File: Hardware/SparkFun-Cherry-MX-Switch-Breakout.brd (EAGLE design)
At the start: 19.1 x 19.1 mm, 17 parts

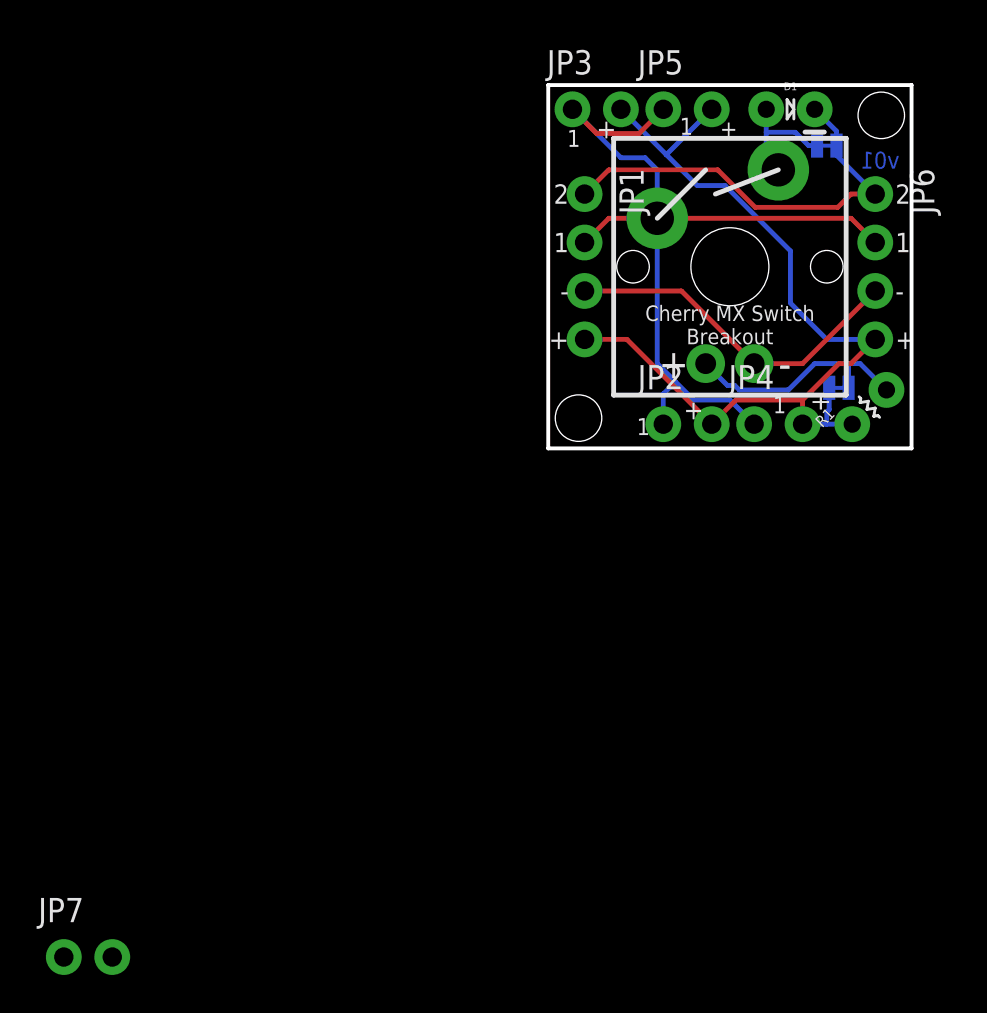
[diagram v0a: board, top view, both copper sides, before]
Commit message: Removing extra 2-pin connector.
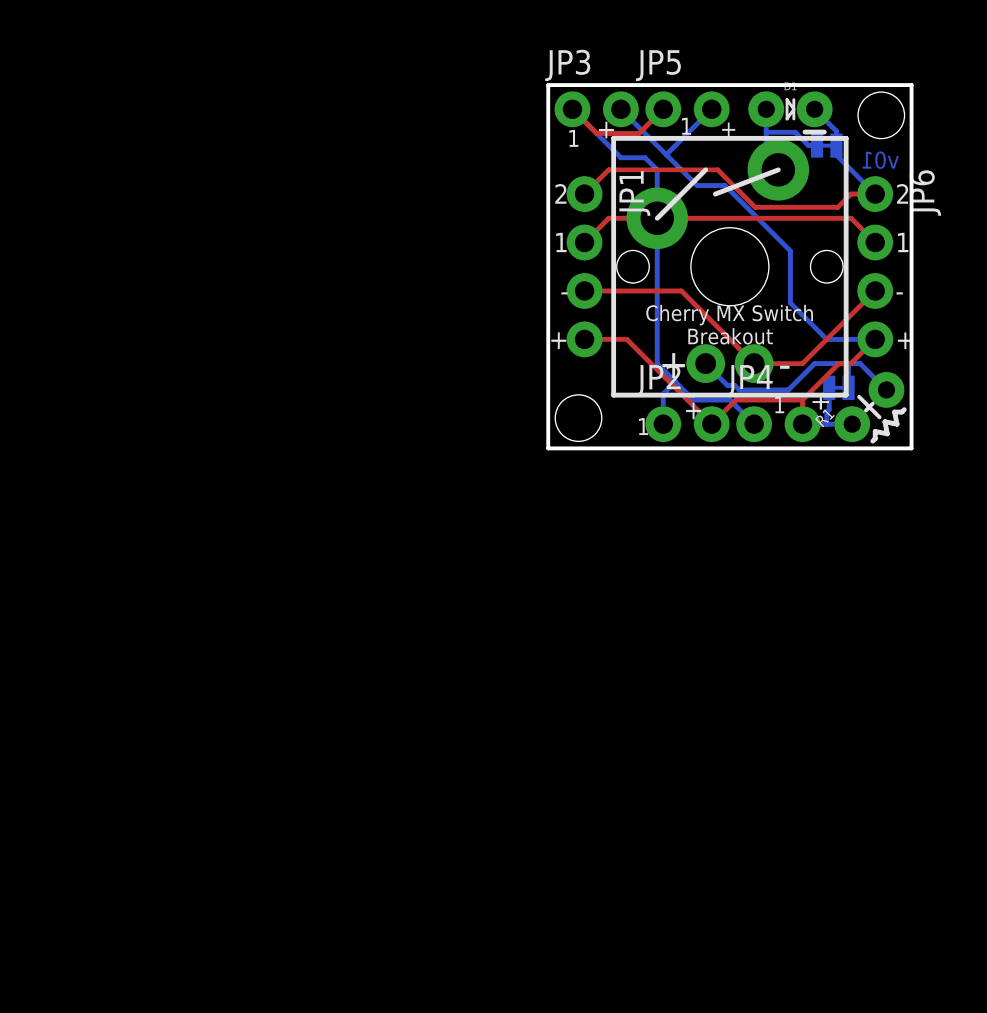
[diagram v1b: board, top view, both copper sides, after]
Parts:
- removed JP7: (no value), SparkFun-Connectors:1X02_NO_SILK
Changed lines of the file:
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@@
 <layer number="47" name="Measures" color="7" fill="1" visible="no" active="yes"/>
 <layer number="48" name="Document" color="7" fill="1" visible="no" active="yes"/>
-<layer number="49" name="Reference" color="7" fill="1" visible="yes" active="yes"/>
+<layer number="49" name="Reference" color="7" fill="1" visible="no" active="yes"/>
 <layer number="50" name="dxf" color="7" fill="1" visible="no" active="no"/>
 <layer number="51" name="tDocu" color="6" fill="1" visible="yes" active="yes"/>
@@
 <wire x1="14.605" y1="3.175" x2="15.875" y2="3.175" width="0.254" layer="30"/>
 <wire x1="15.24" y1="17.399" x2="15.24" y2="18.161" width="0.254" layer="22"/>
+<wire x1="17.018" y1="0.381" x2="17.145" y2="0.508" width="0.254" layer="21"/>
+<wire x1="17.145" y1="0.508" x2="17.145" y2="0.889" width="0.254" layer="21"/>
+<wire x1="17.78" y1="0.762" x2="17.145" y2="0.889" width="0.254" layer="21"/>
+<wire x1="18.669" y1="2.032" x2="18.542" y2="1.905" width="0.254" layer="21"/>
+<wire x1="17.78" y1="0.762" x2="17.653" y2="1.397" width="0.254" layer="21"/>
+<wire x1="18.288" y1="1.27" x2="17.653" y2="1.397" width="0.254" layer="21"/>
+<wire x1="18.288" y1="1.27" x2="18.161" y2="1.905" width="0.254" layer="21"/>
+<wire x1="18.542" y1="1.905" x2="18.161" y2="1.905" width="0.254" layer="21"/>
 </plain>
 <attributes>
@@
 <element name="STANDOFF2" library="cherry-temp" package="STAND-OFF-2-56" value="STAND-OFF2-56" x="1.5875" y="1.5875"/>
 <element name="STANDOFF1" library="cherry-temp" package="STAND-OFF-2-56" value="STAND-OFF2-56" x="17.4625" y="17.4625"/>
-<element name="JP7" library="SparkFun-Connectors" package="1X02_NO_SILK" value="" x="-25.4" y="-26.67"/>
 </elements>
 <signals>

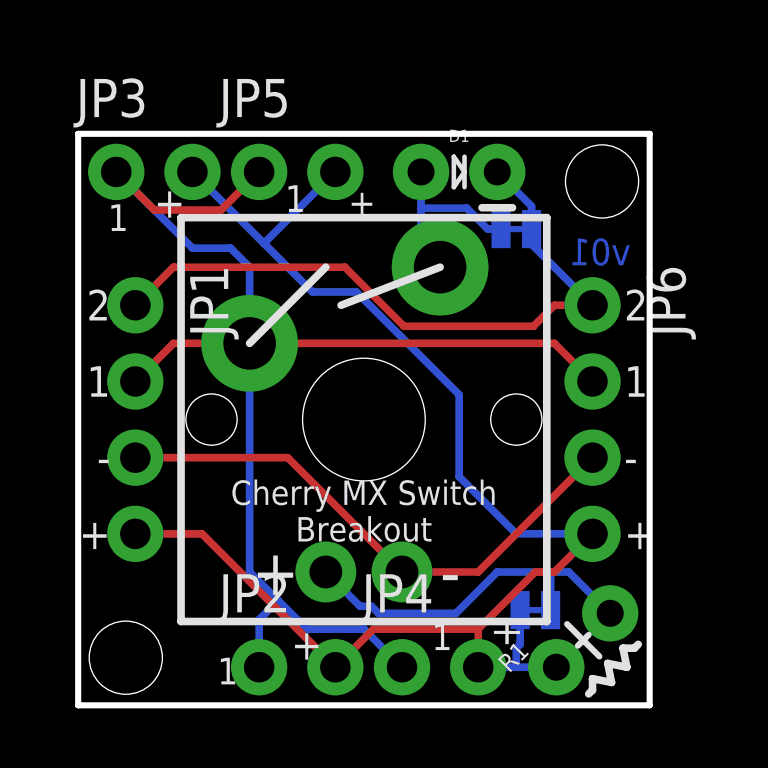
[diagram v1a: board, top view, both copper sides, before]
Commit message: Adjsting some silk, setting version to v10.
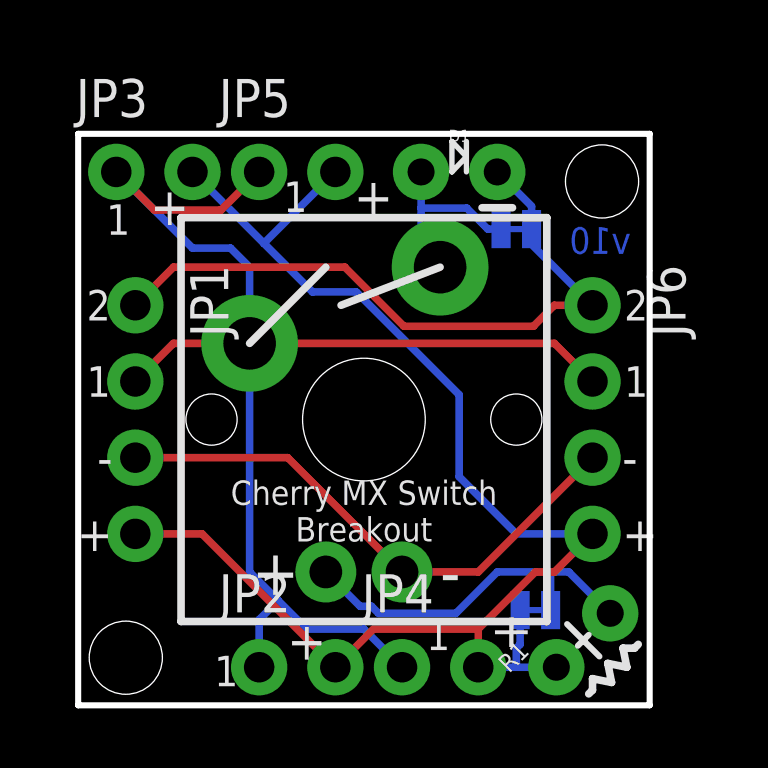
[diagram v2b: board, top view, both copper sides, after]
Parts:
- moved LOGO1 0.57 mm to (4.00, 3.24)
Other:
- board text added: "v10"
- board text removed: "Cherry MX Breakout"
- board text removed: "v01"
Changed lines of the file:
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@@
 <?xml version="1.0" encoding="utf-8"?>
 <!DOCTYPE eagle SYSTEM "eagle.dtd">
-<eagle version="7.1.0">
+<eagle version="7.5.0">
 <drawing>
 <settings>
@@
 <setting verticaltext="up"/>
 </settings>
-<grid distance="0.05" unitdist="inch" unit="inch" style="lines" multiple="1" display="yes" altdistance="0.005" altunitdist="inch" altunit="inch"/>
+<grid distance="0.05" unitdist="inch" unit="inch" style="lines" multiple="1" display="yes" altdistance="0.0025" altunitdist="inch" altunit="inch"/>
 <layers>
 <layer number="1" name="Top" color="4" fill="1" visible="yes" active="yes"/>
@@
 <layer number="47" name="Measures" color="7" fill="1" visible="no" active="yes"/>
 <layer number="48" name="Document" color="7" fill="1" visible="no" active="yes"/>
-<layer number="49" name="Reference" color="7" fill="1" visible="no" active="yes"/>
+<layer number="49" name="Reference" color="7" fill="1" visible="yes" active="yes"/>
 <layer number="50" name="dxf" color="7" fill="1" visible="no" active="no"/>
 <layer number="51" name="tDocu" color="6" fill="1" visible="yes" active="yes"/>
@@
 <text x="2.667" y="13.335" size="1.27" layer="22" font="vector" ratio="15" rot="MR0" align="center-right">2</text>
 <text x="2.667" y="10.795" size="1.27" layer="22" font="vector" ratio="15" rot="MR0" align="center-right">1</text>
-<text x="2.667" y="8.255" size="1.27" layer="22" font="vector" ratio="15" rot="MR0" align="center-right">-</text>
-<text x="2.667" y="5.715" size="1.27" layer="22" font="vector" ratio="15" rot="MR0" align="center-right">+</text>
+<text x="2.667" y="8.255" size="1.778" layer="22" font="vector" ratio="15" rot="MR0" align="center-right">-</text>
+<text x="2.667" y="5.715" size="1.778" layer="22" font="vector" ratio="15" rot="MR0" align="center-right">+</text>
 <text x="16.0655" y="13.335" size="1.27" layer="22" font="vector" ratio="15" rot="MR0" align="center-left">2</text>
 <text x="16.0655" y="10.795" size="1.27" layer="22" font="vector" ratio="15" rot="MR0" align="center-left">1</text>
-<text x="16.0655" y="8.255" size="1.27" layer="22" font="vector" ratio="15" rot="MR0" align="center-left">-</text>
-<text x="16.0655" y="5.715" size="1.27" layer="22" font="vector" ratio="15" rot="MR0" align="center-left">+</text>
+<text x="16.0655" y="8.255" size="1.778" layer="22" font="vector" ratio="15" rot="MR0" align="center-left">-</text>
+<text x="16.0655" y="5.715" size="1.778" layer="22" font="vector" ratio="15" rot="MR0" align="center-left">+</text>
 <text x="5.9055" y="2.286" size="1.27" layer="22" font="vector" ratio="15" rot="MR0" align="bottom-center">1</text>
-<text x="8.4455" y="2.286" size="1.27" layer="22" font="vector" ratio="15" rot="MR0" align="bottom-center">+</text>
+<text x="8.4455" y="2.032" size="1.524" layer="22" font="vector" ratio="15" rot="MR0" align="bottom-center">+</text>
 <text x="10.668" y="2.286" size="1.27" layer="22" font="vector" ratio="15" rot="MR0" align="bottom-center">1</text>
-<text x="13.208" y="2.286" size="1.27" layer="22" font="vector" ratio="15" rot="MR0" align="bottom-center">+</text>
+<text x="13.208" y="2.032" size="1.524" layer="22" font="vector" ratio="15" rot="MR0" align="bottom-center">+</text>
 <text x="1.143" y="16.7005" size="1.27" layer="22" font="vector" ratio="15" rot="MR0" align="top-center">1</text>
-<text x="3.683" y="16.7005" size="1.27" layer="22" font="vector" ratio="15" rot="MR0" align="top-center">+</text>
+<text x="3.683" y="16.8275" size="1.524" layer="22" font="vector" ratio="15" rot="MR0" align="top-center">+</text>
 <text x="5.9055" y="16.7005" size="1.27" layer="22" font="vector" ratio="15" rot="MR0" align="top-center">1</text>
-<text x="8.4455" y="16.7005" size="1.27" layer="22" font="vector" ratio="15" rot="MR0" align="top-center">+</text>
+<text x="8.4455" y="16.8275" size="1.524" layer="22" font="vector" ratio="15" rot="MR0" align="top-center">+</text>
 <text x="1.0795" y="13.335" size="1.016" layer="21" font="vector" ratio="15" align="center-right">2</text>
 <text x="1.0795" y="10.795" size="1.016" layer="21" font="vector" ratio="15" align="center-right">1</text>
-<text x="1.0795" y="8.255" size="1.016" layer="21" font="vector" ratio="15" align="center-right">-</text>
-<text x="1.0795" y="5.715" size="1.016" layer="21" font="vector" ratio="15" align="center-right">+</text>
+<text x="1.143" y="8.255" size="1.143" layer="21" font="vector" ratio="15" align="center-right">-</text>
+<text x="1.143" y="5.715" size="1.143" layer="21" font="vector" ratio="15" align="center-right">+</text>
 <text x="18.1991" y="13.335" size="1.016" layer="21" font="vector" ratio="15" align="center-left">2</text>
 <text x="18.1991" y="10.795" size="1.016" layer="21" font="vector" ratio="15" align="center-left">1</text>
-<text x="18.1991" y="8.255" size="1.016" layer="21" font="vector" ratio="15" align="center-left">-</text>
-<text x="18.1991" y="5.715" size="1.016" layer="21" font="vector" ratio="15" align="center-left">+</text>
-<text x="1.3335" y="16.7005" size="0.889" layer="21" font="vector" ratio="15" align="top-center">1</text>
-<text x="3.048" y="17.272" size="1.016" layer="21" font="vector" ratio="15" align="top-center">+</text>
-<text x="7.239" y="17.3355" size="0.889" layer="21" font="vector" ratio="15" align="top-center">1</text>
-<text x="9.4615" y="17.2085" size="0.889" layer="21" font="vector" ratio="15" align="top-center">+</text>
-<text x="5.334" y="1.143" size="0.889" layer="21" font="vector" ratio="15" align="center-right">1</text>
-<text x="7.62" y="1.524" size="1.016" layer="21" font="vector" ratio="15" align="bottom-center">+</text>
-<text x="12.1285" y="1.8415" size="0.889" layer="21" font="vector" ratio="15" align="bottom-center">1</text>
-<text x="14.224" y="1.905" size="1.016" layer="21" font="vector" ratio="15" rot="R90" align="center-left">+</text>
-<text x="17.399" y="15.113" size="0.889" layer="16" font="vector" ratio="15" rot="MR0" align="center">v01</text>
-<text x="9.525" y="6.604" size="0.8128" layer="22" font="vector" ratio="15" rot="MR0" align="center">Cherry MX
+<text x="18.1356" y="8.255" size="1.143" layer="21" font="vector" ratio="15" align="center-left">-</text>
+<text x="18.1356" y="5.715" size="1.143" layer="21" font="vector" ratio="15" align="center-left">+</text>
+<text x="1.3335" y="16.7005" size="1.016" layer="21" font="vector" ratio="15" align="top-center">1</text>
+<text x="3.048" y="17.272" size="1.27" layer="21" font="vector" ratio="15" align="top-center">+</text>
+<text x="7.239" y="17.4625" size="1.016" layer="21" font="vector" ratio="15" align="top-center">1</text>
+<text x="9.8425" y="17.5895" size="1.27" layer="21" font="vector" ratio="15" align="top-center">+</text>
+<text x="5.334" y="1.143" size="1.016" layer="21" font="vector" ratio="15" align="center-right">1</text>
+<text x="7.62" y="1.524" size="1.27" layer="21" font="vector" ratio="15" align="bottom-center">+</text>
+<text x="12.0015" y="1.8415" size="1.016" layer="21" font="vector" ratio="15" align="bottom-center">1</text>
+<text x="14.351" y="1.778" size="1.27" layer="21" font="vector" ratio="15" rot="R90" align="center-left">+</text>
+<text x="17.399" y="15.494" size="0.889" layer="16" font="vector" ratio="15" rot="MR0" align="center">v10</text>
+<text x="9.525" y="6.477" size="0.8128" layer="22" font="vector" ratio="15" rot="MR0" align="center">Cherry MX Switch
 Breakout</text>
 <text x="9.525" y="6.477" size="0.8128" layer="21" font="vector" ratio="15" align="center">Cherry MX Switch
@@
 <text x="-2.54" y="-7.62" size="0.889" layer="47" font="vector" ratio="15" align="center-right">Units in inches</text>
 <text x="24.13" y="-20.955" size="1.27" layer="51" font="vector" ratio="15" align="center-left">Jim Lindblom</text>
-<text x="15.494" y="4.3815" size="0.8128" layer="22" font="vector" ratio="15" rot="MR180" align="center-right">R</text>
-<text x="14.1605" y="14.732" size="0.8128" layer="22" font="vector" ratio="15" rot="MR0" align="center-right">D</text>
+<text x="15.113" y="3.937" size="1.016" layer="22" font="vector" ratio="15" rot="MR0" align="bottom-center">R</text>
+<text x="14.478" y="15.113" size="1.016" layer="22" font="vector" ratio="15" rot="MR0" align="top-center">D</text>
 <wire x1="13.97" y1="15.875" x2="15.24" y2="15.875" width="0.254" layer="30"/>
 <wire x1="14.605" y1="3.175" x2="15.875" y2="3.175" width="0.254" layer="30"/>
@@
 <wire x1="18.288" y1="1.27" x2="18.161" y2="1.905" width="0.254" layer="21"/>
 <wire x1="18.542" y1="1.905" x2="18.161" y2="1.905" width="0.254" layer="21"/>
+<text x="7.1755" y="4.445" size="1.524" layer="22" font="vector" ratio="15" rot="MR0" align="center-left">+</text>
+<text x="11.6205" y="4.445" size="1.524" layer="22" font="vector" ratio="15" rot="MR180" align="center-left">-</text>
+<wire x1="12.4587" y1="18.796" x2="12.4587" y2="17.78" width="0.1778" layer="21"/>
+<wire x1="12.4587" y1="17.78" x2="12.9413" y2="18.288" width="0.1778" layer="21"/>
+<wire x1="12.9413" y1="18.288" x2="12.4587" y2="18.796" width="0.1778" layer="21"/>
+<wire x1="12.9413" y1="18.796" x2="12.9413" y2="18.288" width="0.1778" layer="21"/>
+<wire x1="12.9413" y1="18.288" x2="12.9413" y2="17.78" width="0.1778" layer="21"/>
 </plain>
 <attributes>
@@
 <element name="JP2" library="SparkFun-Connectors" package="1X02_NO_SILK" value="" x="6.0325" y="1.27"/>
 <element name="LOGO2" library="SparkFun-Aesthetics" package="SFE_LOGO_FLAME_.1" value="SFE_LOGO_FLAME.1_INCH" x="13.335" y="9.652" rot="MR0"/>
-<element name="LOGO1" library="SparkFun-Aesthetics" package="OSHW-LOGO-S" value="OSHW-LOGOS" x="4.2545" y="3.7465" rot="MR0"/>
+<element name="LOGO1" library="SparkFun-Aesthetics" package="OSHW-LOGO-S" value="OSHW-LOGOS" x="4.0005" y="3.2385" rot="MR0"/>
 <element name="STANDOFF2" library="cherry-temp" package="STAND-OFF-2-56" value="STAND-OFF2-56" x="1.5875" y="1.5875"/>
 <element name="STANDOFF1" library="cherry-temp" package="STAND-OFF-2-56" value="STAND-OFF2-56" x="17.4625" y="17.4625"/>
